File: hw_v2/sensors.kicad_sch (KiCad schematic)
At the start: 47 parts, among them U10 BMP280, U21 ADXL343, U23 MCP6004, U24 MCP6004, U6 TJA1051T-3

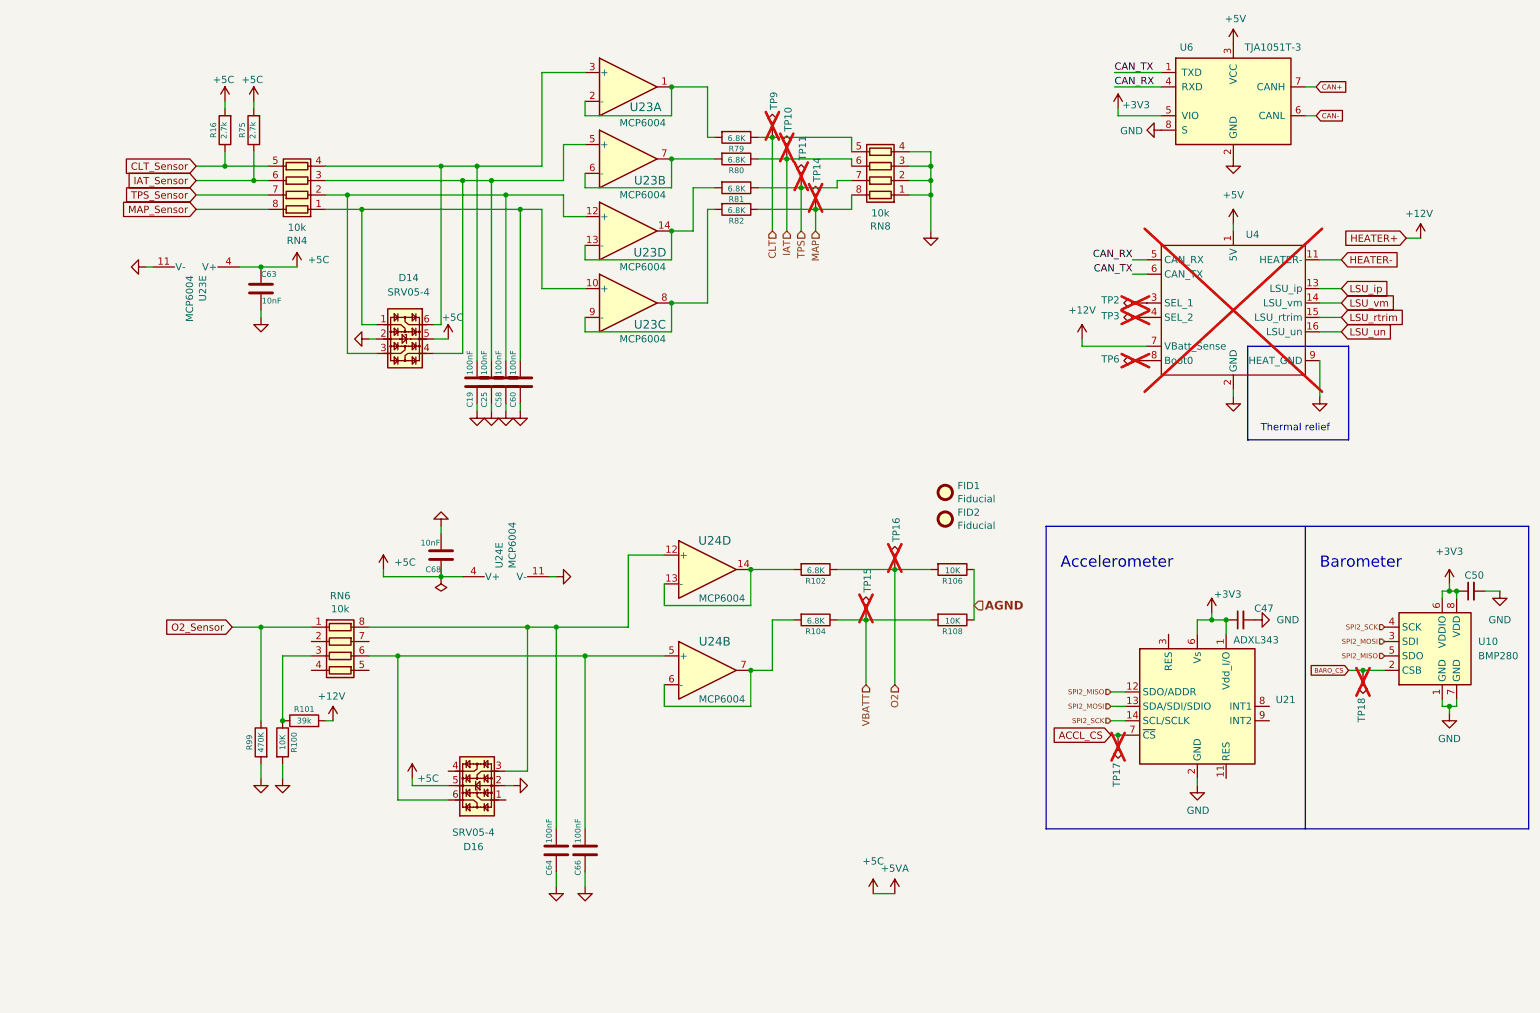
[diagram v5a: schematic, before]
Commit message: Fix some ERC errors
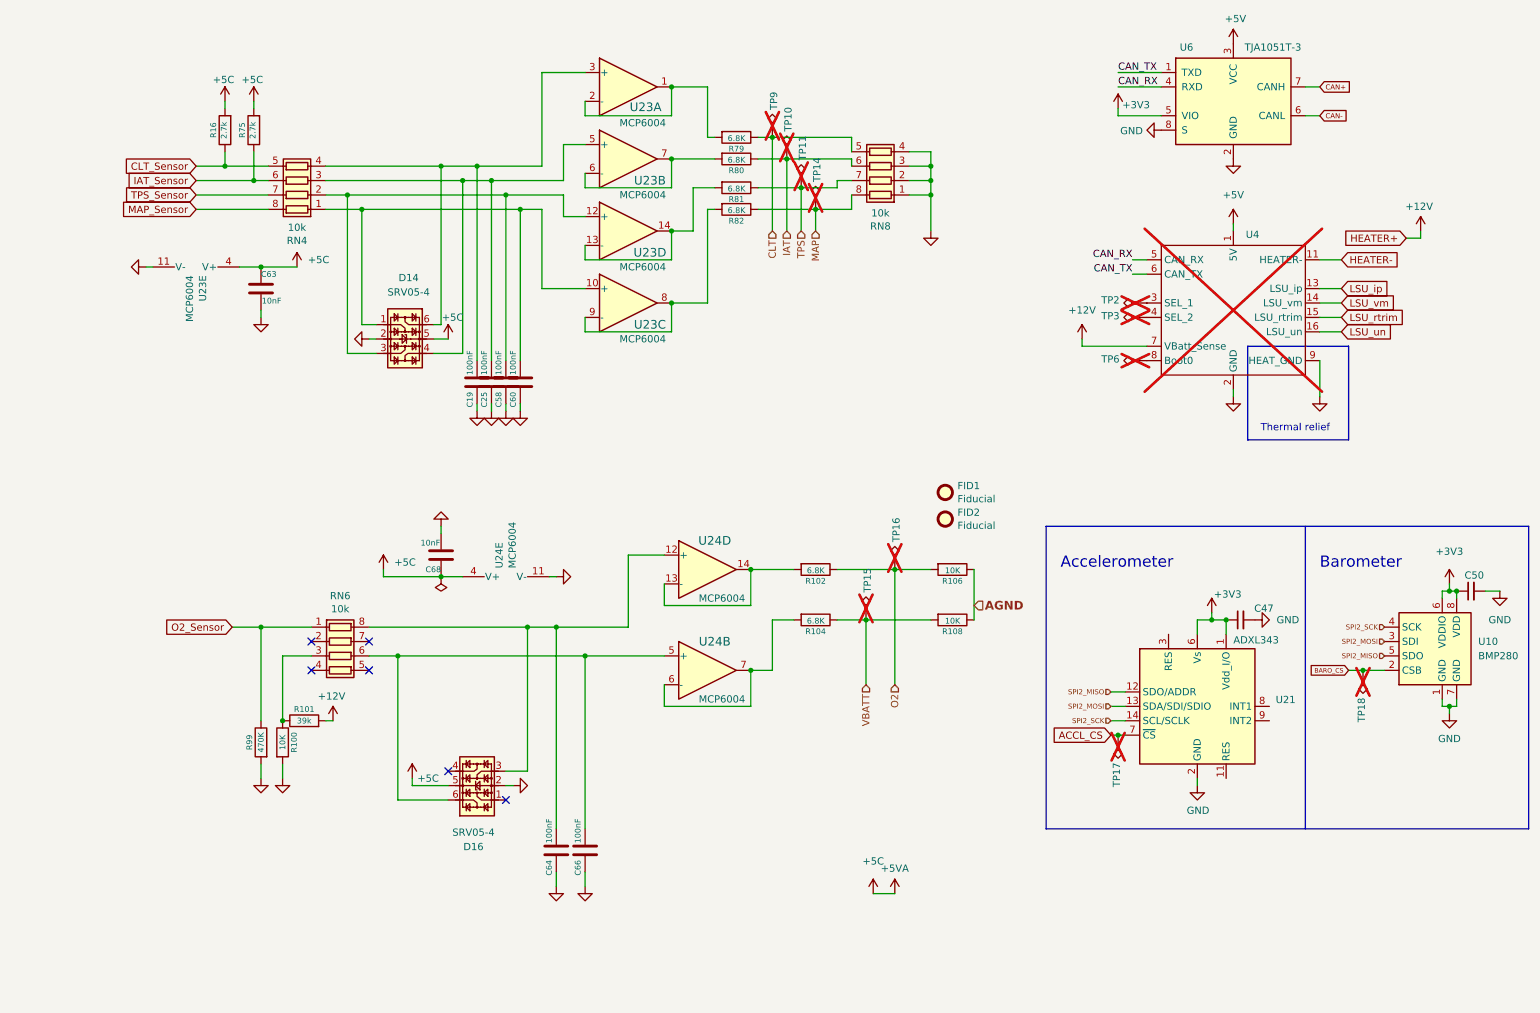
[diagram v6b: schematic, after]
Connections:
- no-connect marks 0 -> 6
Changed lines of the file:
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@@
 		(color 0 0 0 0)
 	)
+	(no_connect
+		(at 66.04 132.08)
+	)
+	(no_connect
+		(at 90.17 154.94)
+	)
+	(no_connect
+		(at 100.33 160.02)
+	)
+	(no_connect
+		(at 76.2 132.08)
+	)
+	(no_connect
+		(at 66.04 137.16)
+	)
+	(no_connect
+		(at 76.2 137.16)
+	)
 	(wire
 		(pts
@@
 	(wire
 		(pts
-			(xy 261.62 60.96) (xy 259.08 60.96)
-		)
-		(stroke
-			(width 0)
-			(type default)
-		)
-	)
-	(wire
-		(pts
 			(xy 152.4 52.07) (xy 158.75 52.07)
 		)
@@
 	(wire
 		(pts
+			(xy 261.62 59.69) (xy 261.62 60.96)
+		)
+		(stroke
+			(width 0)
+			(type default)
+		)
+	)
+	(wire
+		(pts
 			(xy 143.51 137.16) (xy 143.51 143.51)
 		)
@@
 	(wire
 		(pts
-			(xy 207.645 31.75) (xy 215.9 31.75)
+			(xy 208.28 31.75) (xy 215.9 31.75)
 		)
 		(stroke
@@
 	(wire
 		(pts
-			(xy 215.9 34.29) (xy 207.645 34.29)
+			(xy 215.9 34.29) (xy 208.28 34.29)
 		)
 		(stroke
@@
 	(wire
 		(pts
-			(xy 241.3 39.37) (xy 243.205 39.37)
+			(xy 241.3 39.37) (xy 243.84 39.37)
 		)
 		(stroke
@@
 	(wire
 		(pts
+			(xy 261.62 60.96) (xy 259.08 60.96)
+		)
+		(stroke
+			(width 0)
+			(type default)
+		)
+	)
+	(wire
+		(pts
 			(xy 163.83 128.27) (xy 175.26 128.27)
 		)
@@
 	(wire
 		(pts
-			(xy 241.3 34.29) (xy 243.205 34.29)
+			(xy 241.3 34.29) (xy 243.84 34.29)
 		)
 		(stroke
@@
 	)
 	(label "CAN_RX"
-		(at 207.645 34.29 0)
+		(at 208.28 34.29 0)
 		(effects
 			(font
@@
 	)
 	(label "CAN_TX"
-		(at 207.645 31.75 0)
+		(at 208.28 31.75 0)
 		(effects
 			(font
@@
 	(global_label "CAN+"
 		(shape input)
-		(at 243.205 34.29 0)
+		(at 243.84 34.29 0)
 		(effects
 			(font
@@
 		)
 		(property "Intersheetrefs" "${INTERSHEET_REFS}"
-			(at 248.577 34.2345 0)
+			(at 249.212 34.2345 0)
 			(effects
 				(font
@@
 	(global_label "CAN-"
 		(shape input)
-		(at 243.205 39.37 0)
+		(at 243.84 39.37 0)
 		(effects
 			(font
@@
 		)
 		(property "Intersheetrefs" "${INTERSHEET_REFS}"
-			(at 248.577 39.4255 0)
+			(at 249.212 39.4255 0)
 			(effects
 				(font
@@
 			)
 		)
-		(property "Description" ""
+		(property "Description" "Power symbol creates a global label with name \"GND\" , ground"
 			(at 228.6 46.99 0)
 			(effects
@@
 			)
 		)
-		(property "Description" ""
+		(property "Description" "Power symbol creates a global label with name \"+5C\""
 			(at 50.8 36.83 0)
 			(effects
@@
 			)
 		)
-		(property "Description" ""
+		(property "Description" "Power symbol creates a global label with name \"GND\" , ground"
 			(at 175.26 59.69 0)
 			(effects
@@
 			)
 		)
-		(property "Description" ""
+		(property "Description" "Power symbol creates a global label with name \"GND\" , ground"
 			(at 57.15 156.21 0)
 			(effects
@@
 			)
 		)
-		(property "Description" ""
+		(property "Description" "Power symbol creates a global label with name \"+3V3\""
 			(at 224.79 127 0)
 			(effects
@@
 	)
 	(symbol
-		(lib_name "GND_1")
 		(lib_id "power:GND")
 		(at 275.59 123.19 0)
@@
 			)
 		)
-		(property "Description" ""
+		(property "Description" "Power symbol creates a global label with name \"+5V\""
 			(at 228.6 58.42 0)
 			(effects
@@
 			)
 		)
-		(property "Description" ""
+		(property "Description" "Power symbol creates a global label with name \"GND\" , ground"
 			(at 243.84 88.9 0)
 			(effects
@@
 			)
 		)
-		(property "Description" ""
+		(property "Description" "Power symbol creates a global label with name \"GND\" , ground"
 			(at 76.2 78.74 0)
 			(effects
@@
 			)
 		)
-		(property "Description" ""
+		(property "Description" "Power symbol creates a global label with name \"GND\" , ground"
 			(at 36.83 66.04 0)
 			(effects
@@
 			)
 		)
-		(property "Description" ""
+		(property "Description" "Power symbol creates a global label with name \"+3V3\""
 			(at 208.28 38.1 0)
 			(effects
@@
 			)
 		)
-		(property "Description" ""
+		(property "Description" "Power symbol creates a global label with name \"GND\" , ground"
 			(at 100.33 91.44 0)
 			(effects
@@
 			)
 		)
-		(property "Description" ""
+		(property "Description" "Power symbol creates a global label with name \"+5C\""
 			(at 165.1 176.53 0)
 			(effects
@@
 			)
 		)
-		(property "Description" ""
+		(property "Description" "Power symbol creates a global label with name \"+5V\""
 			(at 228.6 26.67 0)
 			(effects
@@
 			)
 		)
-		(property "Description" ""
+		(property "Description" "Power symbol creates a global label with name \"GND\" , ground"
 			(at 114.3 175.26 0)
 			(effects
@@
 			)
 		)
-		(property "Description" ""
+		(property "Description" "Power symbol creates a global label with name \"+5C\""
 			(at 55.88 36.83 0)
 			(effects
@@
 			)
 		)
-		(property "Description" ""
+		(property "Description" "Power symbol creates a global label with name \"GND\" , ground"
 			(at 222.25 157.48 0)
 			(effects
@@
 			)
 		)
-		(property "Description" ""
+		(property "Description" "Power symbol creates a global label with name \"GND\" , ground"
 			(at 88.9 111.76 0)
 			(effects
@@
 	)
 	(symbol
-		(lib_name "GND_1")
 		(lib_id "power:GND")
 		(at 232.41 128.27 90)
@@
 			)
 		)
-		(property "Description" ""
+		(property "Description" "Power symbol creates a global label with name \"GND\" , ground"
 			(at 109.22 120.65 0)
 			(effects
@@
 			)
 		)
-		(property "Description" ""
+		(property "Description" "Power symbol creates a global label with name \"GND\" , ground"
 			(at 97.79 91.44 0)
 			(effects
@@
 			)
 		)
-		(property "Description" ""
+		(property "Description" "Power symbol creates a global label with name \"+3V3\""
 			(at 266.7 121.92 0)
 			(effects
@@
 			)
 		)
-		(property "Description" ""
+		(property "Description" "Power symbol creates a global label with name \"GND\" , ground"
 			(at 95.25 91.44 0)
 			(effects
@@
 			)
 		)
-		(property "Description" ""
+		(property "Description" "Power symbol creates a global label with name \"+5C\""
 			(at 90.17 78.74 0)
 			(effects
@@
 			)
 		)
-		(property "Description" ""
+		(property "Description" "Power symbol creates a global label with name \"GND\" , ground"
 			(at 266.7 144.78 0)
 			(effects
@@
 			)
 		)
-		(property "Description" ""
+		(property "Description" "Power symbol creates a global label with name \"GND\" , ground"
 			(at 228.6 88.9 0)
 			(effects
@@
 			)
 		)
-		(property "Description" ""
+		(property "Description" "Power symbol creates a global label with name \"GND\" , ground"
 			(at 109.22 175.26 0)
 			(effects
@@
 			)
 		)
-		(property "Description" ""
+		(property "Description" "Power symbol creates a global label with name \"GND\" , ground"
 			(at 57.15 74.93 0)
 			(effects
@@
 		(lib_name "+12V_1")
 		(lib_id "power:+12V")
-		(at 261.62 60.96 0)
+		(at 261.62 59.69 0)
 		(unit 1)
 		(exclude_from_sim no)
@@
 		(dnp no)
 		(property "Reference" "#PWR032"
-			(at 261.62 64.77 0)
+			(at 261.62 63.5 0)
 			(effects
 				(font
@@
 		)
 		(property "Value" "+12V"
-			(at 261.366 56.642 0)
+			(at 261.366 55.372 0)
 			(effects
 				(font
@@
 		)
 		(property "Footprint" ""
-			(at 261.62 60.96 0)
+			(at 261.62 59.69 0)
 			(effects
 				(font
@@
 		)
 		(property "Datasheet" ""
-			(at 261.62 60.96 0)
+			(at 261.62 59.69 0)
 			(effects
 				(font
@@
 		)
 		(property "Description" "Power symbol creates a global label with name \"+12V\""
-			(at 261.62 60.96 0)
+			(at 261.62 59.69 0)
 			(effects
 				(font
@@
 			)
 		)
-		(property "Description" ""
+		(property "Description" "Power symbol creates a global label with name \"GND\" , ground"
 			(at 101.6 157.48 0)
 			(effects
@@
 			)
 		)
-		(property "Description" ""
+		(property "Description" "Power symbol creates a global label with name \"GND\" , ground"
 			(at 60.96 156.21 0)
 			(effects
@@
 			)
 		)
-		(property "Description" ""
+		(property "Description" "Power symbol creates a global label with name \"+5C\""
 			(at 63.5 66.04 0)
 			(effects
@@
 			)
 		)
-		(property "Description" ""
+		(property "Description" "Power symbol creates a global label with name \"GND\" , ground"
 			(at 215.9 41.91 0)
 			(effects
@@
 			)
 		)
-		(property "Description" ""
+		(property "Description" "Power symbol creates a global label with name \"GND\" , ground"
 			(at 102.87 91.44 0)
 			(effects
@@
 			)
 		)
-		(property "Description" ""
+		(property "Description" "Power symbol creates a global label with name \"+5C\""
 			(at 78.74 119.38 0)
 			(effects
@@
 			)
 		)
-		(property "Description" ""
+		(property "Description" "Power symbol creates a global label with name \"+5C\""
 			(at 83.82 156.21 0)
 			(effects

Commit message: planito mas catolico
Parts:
- removed U4: ~, hw_v2lib:WBO-module, symbol OpenEFI_LIB:RusEFI_WBO
- added unit 1 of U24
- added unit 3 of U24
- added U4: ~, symbol hw_v2:WBO_module
- D14, D16: footprint Package_TO_SOT_SMD:SOT-23-6 -> Package_TO_SOT_SMD:SOT-363_SC-70-6
- U6: footprint Package_SO:SOP-8_3.9x4.9mm_P1.27mm -> Package_SO:SOIC-8_3.9x4.9mm_P1.27mm
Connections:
- net AGND is gone; now on net GND: R106.1, R108.1
- net +12V: now also U4.7 (VBatt_Sense)
- net +5V: now also U4.1 (5V)
- net CAN_RX: now also U4.5 (CAN_RX)
- net CAN_TX: now also U4.6 (CAN_TX)
- net GND: now also U4.10 (HEAT_GND2), U4.2 (GND), U4.9 (HEAT_GND)
- net HEATER-: now also U4.11 (HEATER-), U4.12 (HEATER-)
- net LSU_ip: now also U4.13 (LSU_ip)
- net LSU_rtrim: now also U4.15 (LSU_rtrim)
- net LSU_un: now also U4.16 (LSU_un)
- net LSU_vm: now also U4.14 (LSU_vm)
- net at TP2.1: now also U4.3 (SEL_1)
- net at TP3.1: now also U4.4 (SEL_2)
- net at TP6.1: now also U4.8 (Boot0)
- no-connect marks 6 -> 16

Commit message: wip CKP/CMP
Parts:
- U4: footprint (none) -> hw_v2lib:WBO-module
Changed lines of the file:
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@@
 (kicad_sch
-	(version 20241004)
+	(version 20241209)
 	(generator "eeschema")
 	(generator_version "8.99")
@@
 			)
 		)
-		(property "Footprint" ""
+		(property "Footprint" "hw_v2lib:WBO-module"
 			(at 227.33 72.39 0)
 			(effects
